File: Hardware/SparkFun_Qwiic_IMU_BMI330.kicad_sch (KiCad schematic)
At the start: 29 parts, among them J1 Qwiic_RA, J2 Qwiic_RA, J3 Conn_01x06, J4 Conn_01x02, U1 BMI330

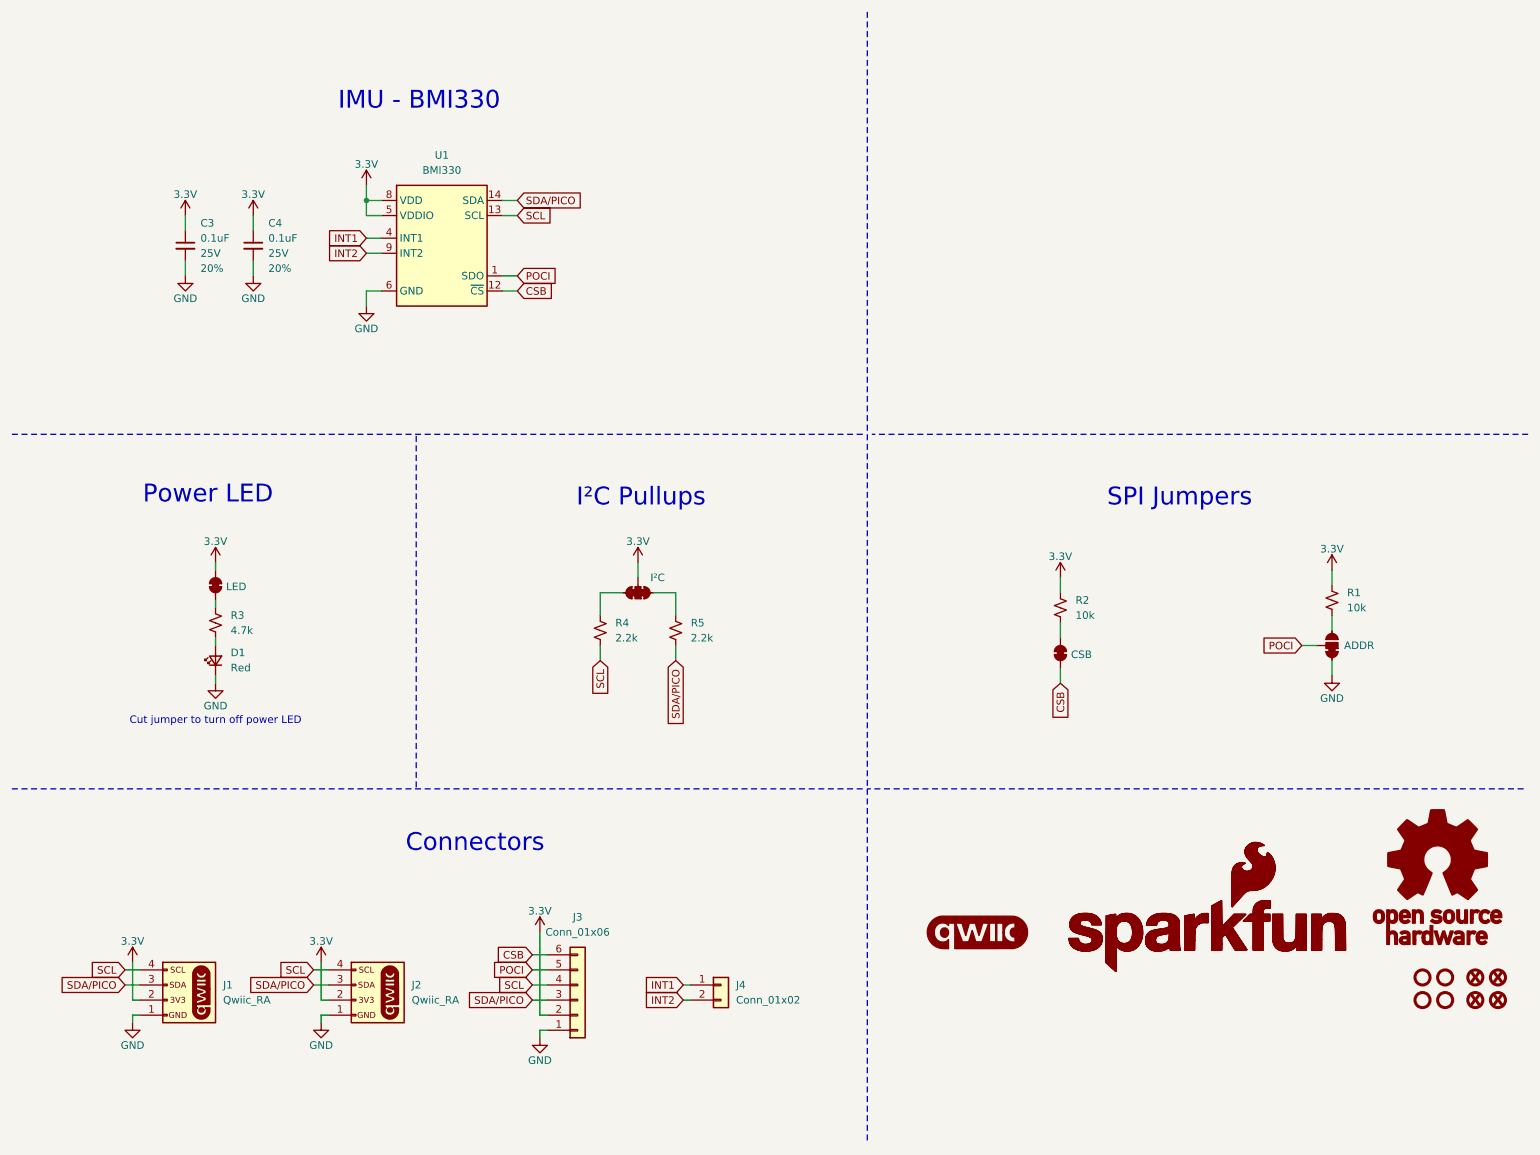
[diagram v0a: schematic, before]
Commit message: Updated designs based on design review
- Nudged traces and vias
- Centered PTH
- Added Silkscreen for I2C/SPI
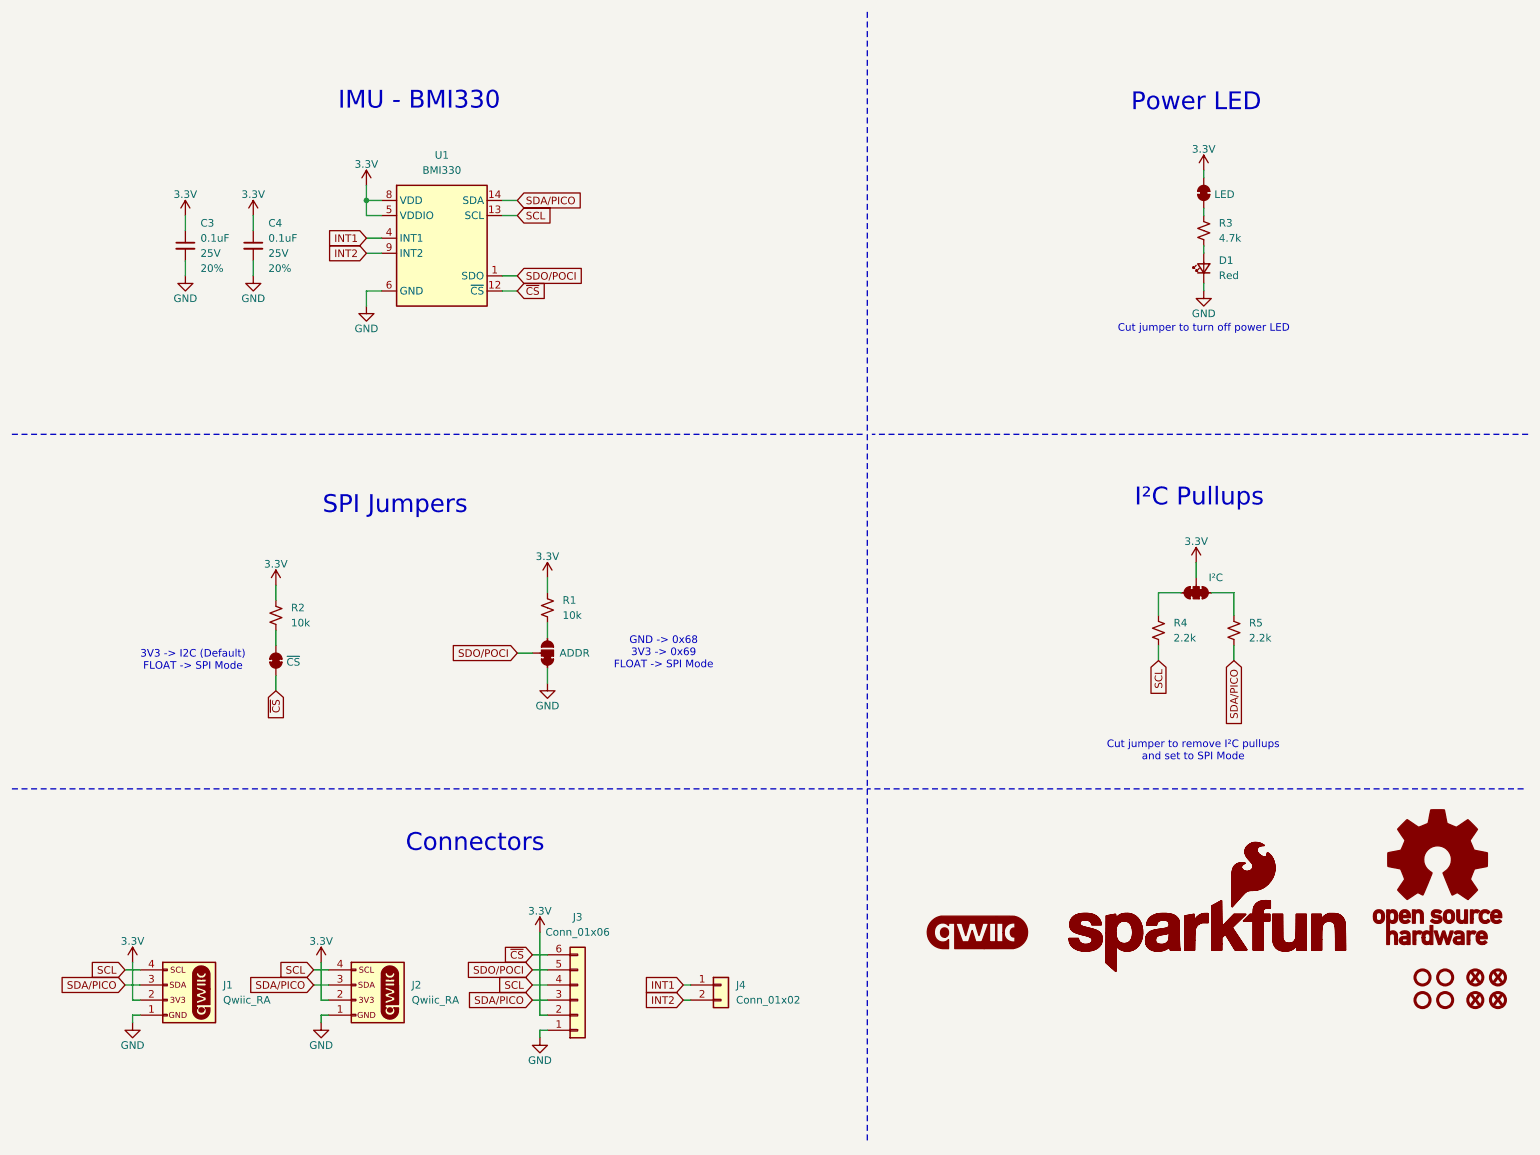
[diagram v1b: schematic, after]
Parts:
- JP3: value CSB -> ~{CS}
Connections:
- net CSB renamed ~{CS}
- net POCI renamed SDO/POCI
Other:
- note added: "3V3 -> I2C (Default) FLOAT -> SPI Mode"
- note added: "Cut jumper to remove I²C pullups and set to SPI Mode"
- note added: "GND -> 0x68 3V3 -> 0x69 FLOAT -> SPI Mode"
- moved on the sheet: D1, R1, R2, R3, R4, R5

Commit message: Changed IC PROD_ID and updated silk to v10
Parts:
- U1: PROD_ID IC-18009 -> IC-28800
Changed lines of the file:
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@@
 			)
 		)
-		(property "PROD_ID" "IC-18009"
+		(property "PROD_ID" "IC-28800"
 			(at 85.09 71.12 0)
 			(effects
